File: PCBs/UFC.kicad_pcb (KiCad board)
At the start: 2 copper layers, 70 parts, among them J1 8 Pin Connector, SW1 SW_SPST, SW10 SW_SPST, SW11 SW_SPST, SW12 SW_SPST, SW13 SW_SPST, SW14 SW_SPST, SW15 SW_SPST, SW16 SW_SPST, SW17 SW_SPST, SW2 SW_SPST, SW3 SW_SPST, SW4 SW_SPST, SW5 SW_SPST, SW6 SW_SPST, SW7 SW_SPST, SW8 SW_SPST, SW9 SW_SPST, U1 STM32F103C8T6, U2 HT1632C-52LQFP, U3 HT1632C-52LQFP

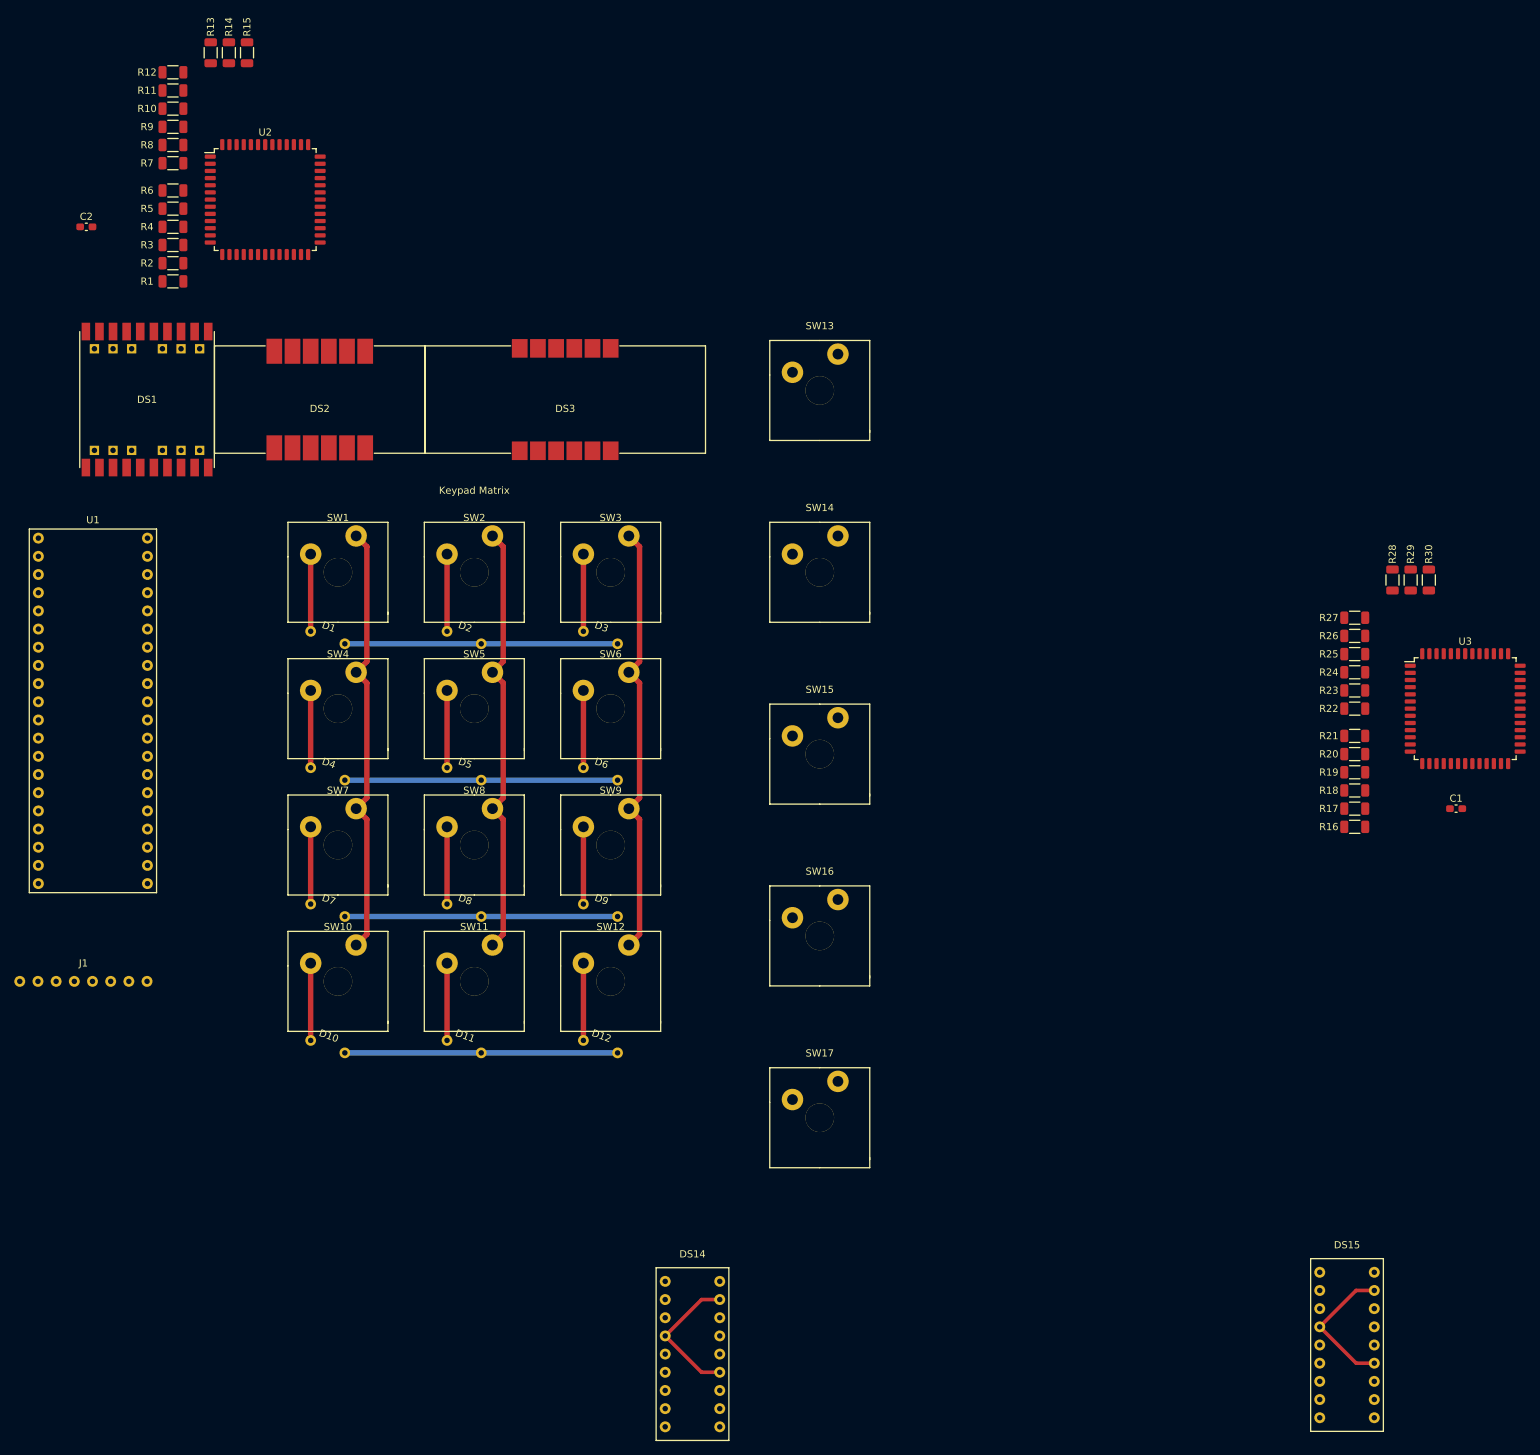
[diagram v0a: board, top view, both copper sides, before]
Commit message: Split up board, started routing traces
Moved the LED drivers and the STM32 board off of the main board and onto a daughterboard to fit a reasonable space. Second board will go behind the first, connected with .1" headers. 
Additionally, traces on the bottom four (second LED driver) OPT displays are routed. 
Redid the OPT buttons to be included in the keypad matrix, to save pins.
Removed the shift register pins and wired it all directly to the STM32, to save space
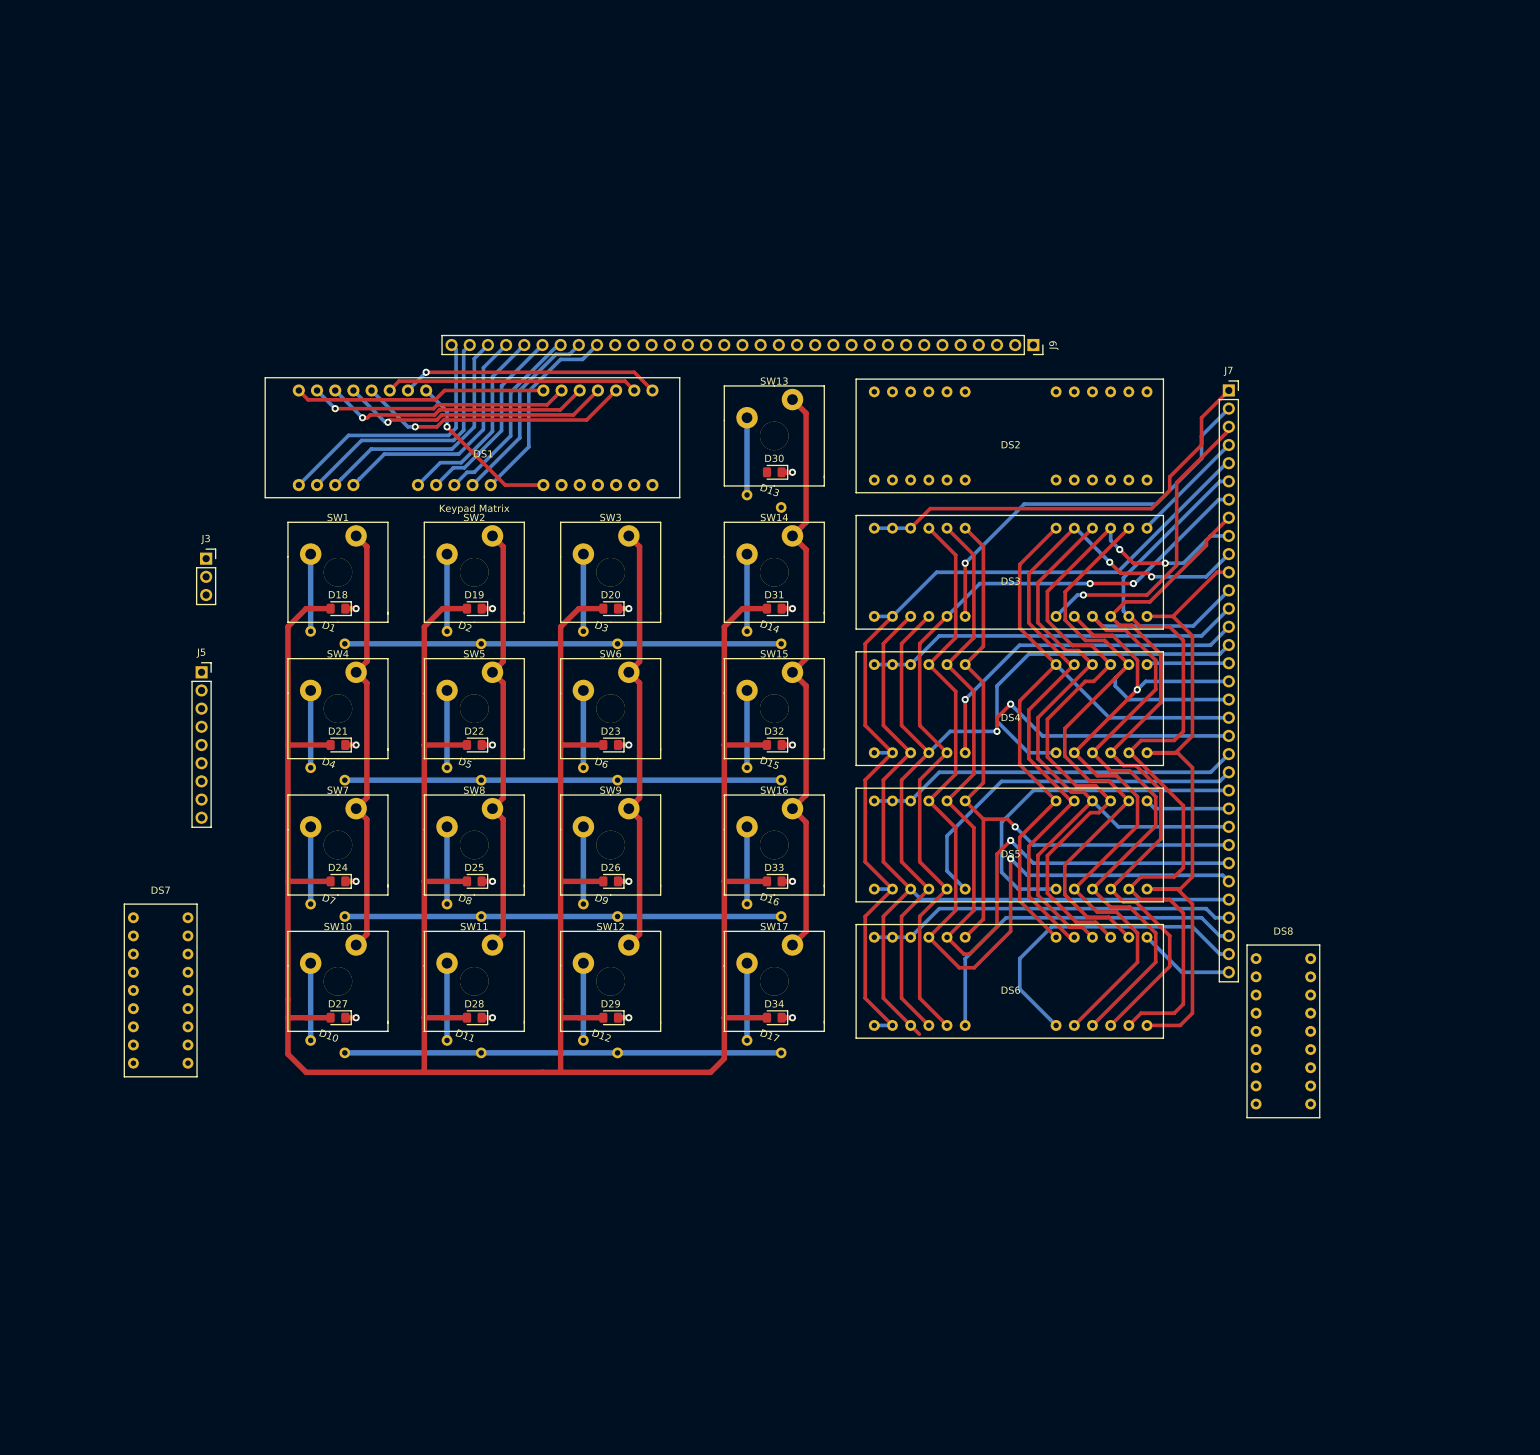
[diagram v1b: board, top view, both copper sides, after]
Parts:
- removed C1, C2: .1uF, Capacitor_SMD:C_0603_1608Metric_Pad1.08x0.95mm_HandSolder
- removed DS14, DS15: 14SegDisplayLumex, UFC:LDS-F3902RI
- removed J1: 8 Pin Connector, UFC:8pin254mm
- removed R1, R10, R11, R12, R13, R14, R15, R16, R17, R18, R19, R2, R20, R21, R22, R23, R24, R25, R26, R27, R28, R29, R3, R30, R4, R5, R6, R7, R8, R9: 520R, Resistor_SMD:R_1206_3216Metric
- removed U1: STM32F103C8T6, UFC:Bluepill
- removed U2, U3: HT1632C-52LQFP, Package_QFP:LQFP-52_14x14mm_P1mm
- added D13: D, Keypad:1N4148, F.Cu at (149.7, 76.2)
- added D14: D, Keypad:1N4148, F.Cu at (149.7, 95.2)
- added D15: D, Keypad:1N4148, F.Cu at (149.7, 114.3)
- added D16: D, Keypad:1N4148, F.Cu at (149.7, 133.3)
- added D17: D, Keypad:1N4148, F.Cu at (149.7, 152.4)
- added D18: LED, LED_SMD:LED_0805_2012Metric_Pad1.15x1.40mm_HandSolder, F.Cu at (91.4, 87.6)
- added D19: LED, LED_SMD:LED_0805_2012Metric_Pad1.15x1.40mm_HandSolder, F.Cu at (110.5, 87.6)
- added D20: LED, LED_SMD:LED_0805_2012Metric_Pad1.15x1.40mm_HandSolder, F.Cu at (129.5, 87.6)
- added D21: LED, LED_SMD:LED_0805_2012Metric_Pad1.15x1.40mm_HandSolder, F.Cu at (91.4, 106.7)
- added D22: LED, LED_SMD:LED_0805_2012Metric_Pad1.15x1.40mm_HandSolder, F.Cu at (110.5, 106.7)
- added D23: LED, LED_SMD:LED_0805_2012Metric_Pad1.15x1.40mm_HandSolder, F.Cu at (129.5, 106.7)
- added D24: LED, LED_SMD:LED_0805_2012Metric_Pad1.15x1.40mm_HandSolder, F.Cu at (91.4, 125.7)
- added D25: LED, LED_SMD:LED_0805_2012Metric_Pad1.15x1.40mm_HandSolder, F.Cu at (110.5, 125.7)
- added D26: LED, LED_SMD:LED_0805_2012Metric_Pad1.15x1.40mm_HandSolder, F.Cu at (129.5, 125.7)
- added D27: LED, LED_SMD:LED_0805_2012Metric_Pad1.15x1.40mm_HandSolder, F.Cu at (91.4, 144.8)
- added D28: LED, LED_SMD:LED_0805_2012Metric_Pad1.15x1.40mm_HandSolder, F.Cu at (110.5, 144.8)
- added D29: LED, LED_SMD:LED_0805_2012Metric_Pad1.15x1.40mm_HandSolder, F.Cu at (129.5, 144.8)
- added D30: LED, LED_SMD:LED_0805_2012Metric_Pad1.15x1.40mm_HandSolder, F.Cu at (152.4, 68.6)
- added D31: LED, LED_SMD:LED_0805_2012Metric_Pad1.15x1.40mm_HandSolder, F.Cu at (152.4, 87.6)
- added D32: LED, LED_SMD:LED_0805_2012Metric_Pad1.15x1.40mm_HandSolder, F.Cu at (152.4, 106.7)
- added D33: LED, LED_SMD:LED_0805_2012Metric_Pad1.15x1.40mm_HandSolder, F.Cu at (152.4, 125.7)
- added D34: LED, LED_SMD:LED_0805_2012Metric_Pad1.15x1.40mm_HandSolder, F.Cu at (152.4, 144.8)
- added DS4: CustomOptPanel, UFC:OPTDisplay, F.Cu at (185.4, 101.6)
- added DS5: CustomOptPanel, UFC:OPTDisplay, F.Cu at (185.4, 120.7)
- added DS6: CustomOptPanel, UFC:OPTDisplay, F.Cu at (185.4, 139.7)
- added DS7: 14SegDisplayLumex, UFC:LDS-F3902RI, F.Cu at (66.7, 128.3)
- added DS8: 14SegDisplayLumex, UFC:LDS-F3902RI, F.Cu at (223.5, 134.0)
- added J3: Power, Connector_PinSocket_2.54mm:PinSocket_1x03_P2.54mm_Vertical, F.Cu at (73.0, 80.6)
- added J5: Matrix, Connector_PinSocket_2.54mm:PinSocket_1x09_P2.54mm_Vertical, F.Cu at (72.4, 96.5)
- added J7: Driver output 2, Connector_PinSocket_2.54mm:PinSocket_1x33_P2.54mm_Vertical, F.Cu at (215.9, 57.1)
- added J9: Driver output 1, Connector_PinSocket_2.54mm:PinSocket_1x33_P2.54mm_Vertical, F.Cu at (188.6, 50.8)
- DS1: value 14Segx2ChromeLED -> Scratchpad; footprint UFC:SDDCN40G2W -> UFC:Scratchpad
- DS2: value 7Segx3ChromeLED -> CustomOptPanel; footprint UFC:SDTC39G2W -> UFC:OPTDisplay
- DS3: value 7Segx4ChromeLED -> CustomOptPanel; footprint UFC:SDQC39G2W -> UFC:OPTDisplay
- moved DS2 96.7 mm to (185.4, 63.5)
- moved DS3 66.7 mm to (185.4, 82.5)
- moved DS1 47.3 mm to (111.8, 63.5)
- moved SW17 20.1 mm to (152.4, 130.8)
- moved SW16 14.2 mm to (152.4, 111.8)
- moved SW15 8.98 mm to (152.4, 92.7)
- moved SW13 8.98 mm to (152.4, 54.6)
- moved SW14 6.35 mm to (152.4, 73.7)
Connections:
- net /GND renamed /COL4
- DS1 pad 1: /Displays/P1 -> /A1
- DS1 pad 10: /Displays/DP1 -> /B1
- DS1 pad 11: /Displays/C1 -> /C1
- DS1 pad 12: /Displays/D1 -> /D1
- DS1 pad 13: /Displays/E1 -> /E1
- DS1 pad 14: /Displays/C1 -> /F1
- DS1 pad 15: /Displays/D1 -> /G1
- DS1 pad 16: /Displays/E1 -> /COM0-1
- DS1 pad 17: /Displays/G1 -> /COM1-1
- DS1 pad 18: /Displays/A1 -> /COM2-1
- DS1 pad 19: /Displays/B1 -> /COM3-1
- DS1 pad 2: /Displays/N1 -> /B1
- DS1 pad 20: /Displays/G1 -> /COM4-1
- DS1 pad 21: /Displays/A1 -> /COM5-1
- DS1 pad 22: /Displays/B1 -> /COM6-1
- DS1 pad 23: /Displays/K1 -> /COM7-1
- DS1 pad 24: /Displays/J1 -> /COM8-1
- DS1 pad 25: /Displays/COM1-1 -> /H1
- DS1 pad 26: /Displays/H1 -> /J2
- DS1 pad 27: /Displays/F1 -> /K2
- DS1 pad 28: /Displays/K1 -> /L2
- DS1 pad 29: /Displays/J1 -> /M2
- DS1 pad 3: /Displays/M1 -> /C1
- DS1 pad 30: /Displays/COM0-1 -> /N2
- DS1 pad 31: /Displays/H1 -> /P2
- DS1 pad 4: /Displays/L1 -> /D1
- DS1 pad 5: /Displays/DP1 -> /E1
- DS1 pad 6: /Displays/P1 -> /F1
- DS1 pad 7: /Displays/N1 -> /G1
- DS1 pad 8: /Displays/M1 -> /H1
- DS1 pad 9: /Displays/L1 -> /A1
- DS2 pad 1: /Displays/COM2-1 -> /COM9-1
- DS2 pad 10: /Displays/COM3-1 -> /N1
- DS2 pad 11: /Displays/F1 -> /Q1
- DS2 pad 12: Net-(DS2-Pad12) -> /COM12-1
- DS2 pad 2: /Displays/DP1 -> /COM9-1
- DS2 pad 3: /Displays/D1 -> /COM9-1
- DS2 pad 4: /Displays/C1 -> /B1
- DS2 pad 5: /Displays/G1 -> /C1
- DS2 pad 6: /Displays/E1 -> /D1
- DS2 pad 7: /Displays/COM4-1 -> /G1
- DS2 pad 8: /Displays/B1 -> /M1
- DS2 pad 9: /Displays/A1 -> /L1
- DS3 pad 1: /Displays/E1 -> /COM0-2
- DS3 pad 10: /Displays/F1 -> /N2
- DS3 pad 11: /Displays/A1 -> /Q2
- DS3 pad 12: /Displays/COM5-1 -> /COM3-2
- DS3 pad 2: /Displays/D1 -> /COM0-2
- DS3 pad 3: /Displays/DP1 -> /COM0-2
- DS3 pad 4: /Displays/C1 -> /B2
- DS3 pad 5: /Displays/G1 -> /C2
- DS3 pad 6: /Displays/COM8-1 -> /D2
- DS3 pad 7: /Displays/B1 -> /G2
- DS3 pad 8: /Displays/COM7-1 -> /M2
- DS3 pad 9: /Displays/COM6-1 -> /L2
- SW13 pad 1: /SW13 -> Net-(D13-Pad2)
- SW14 pad 1: /SW14 -> Net-(D14-Pad2)
- SW15 pad 1: /SW15 -> Net-(D15-Pad2)
- SW16 pad 1: /SW16 -> Net-(D16-Pad2)
- SW17 pad 1: /SW17 -> Net-(D17-Pad2)
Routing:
- net /LEDPWM: track 0.00 -> 406.8 mm
- net /DOT2: track 0.00 -> 132.6 mm
- net /B2: track 0.00 -> 123.7 mm, vias 0 -> 1
- net /C2: track 0.00 -> 120.7 mm, vias 0 -> 1
- net /DP2: track 0.00 -> 115.3 mm
- net /E2: track 0.00 -> 114.7 mm, vias 0 -> 2
- net /A2: track 0.00 -> 113.4 mm
- net /H2: track 0.00 -> 112.7 mm, vias 0 -> 2
- net /N2: track 0.00 -> 106.8 mm, vias 0 -> 2
- net /K2: track 0.00 -> 105.6 mm
- net /Q2: track 0.00 -> 104.8 mm
- net /P2: track 0.00 -> 103.0 mm
- net /L2: track 0.00 -> 100.3 mm
- net /M2: track 0.00 -> 99.6 mm, vias 0 -> 2
- net /D2: track 0.00 -> 99.3 mm, vias 0 -> 1
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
